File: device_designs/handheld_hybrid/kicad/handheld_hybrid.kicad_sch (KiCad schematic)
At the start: 12 parts, among them U3V3 TPS62864

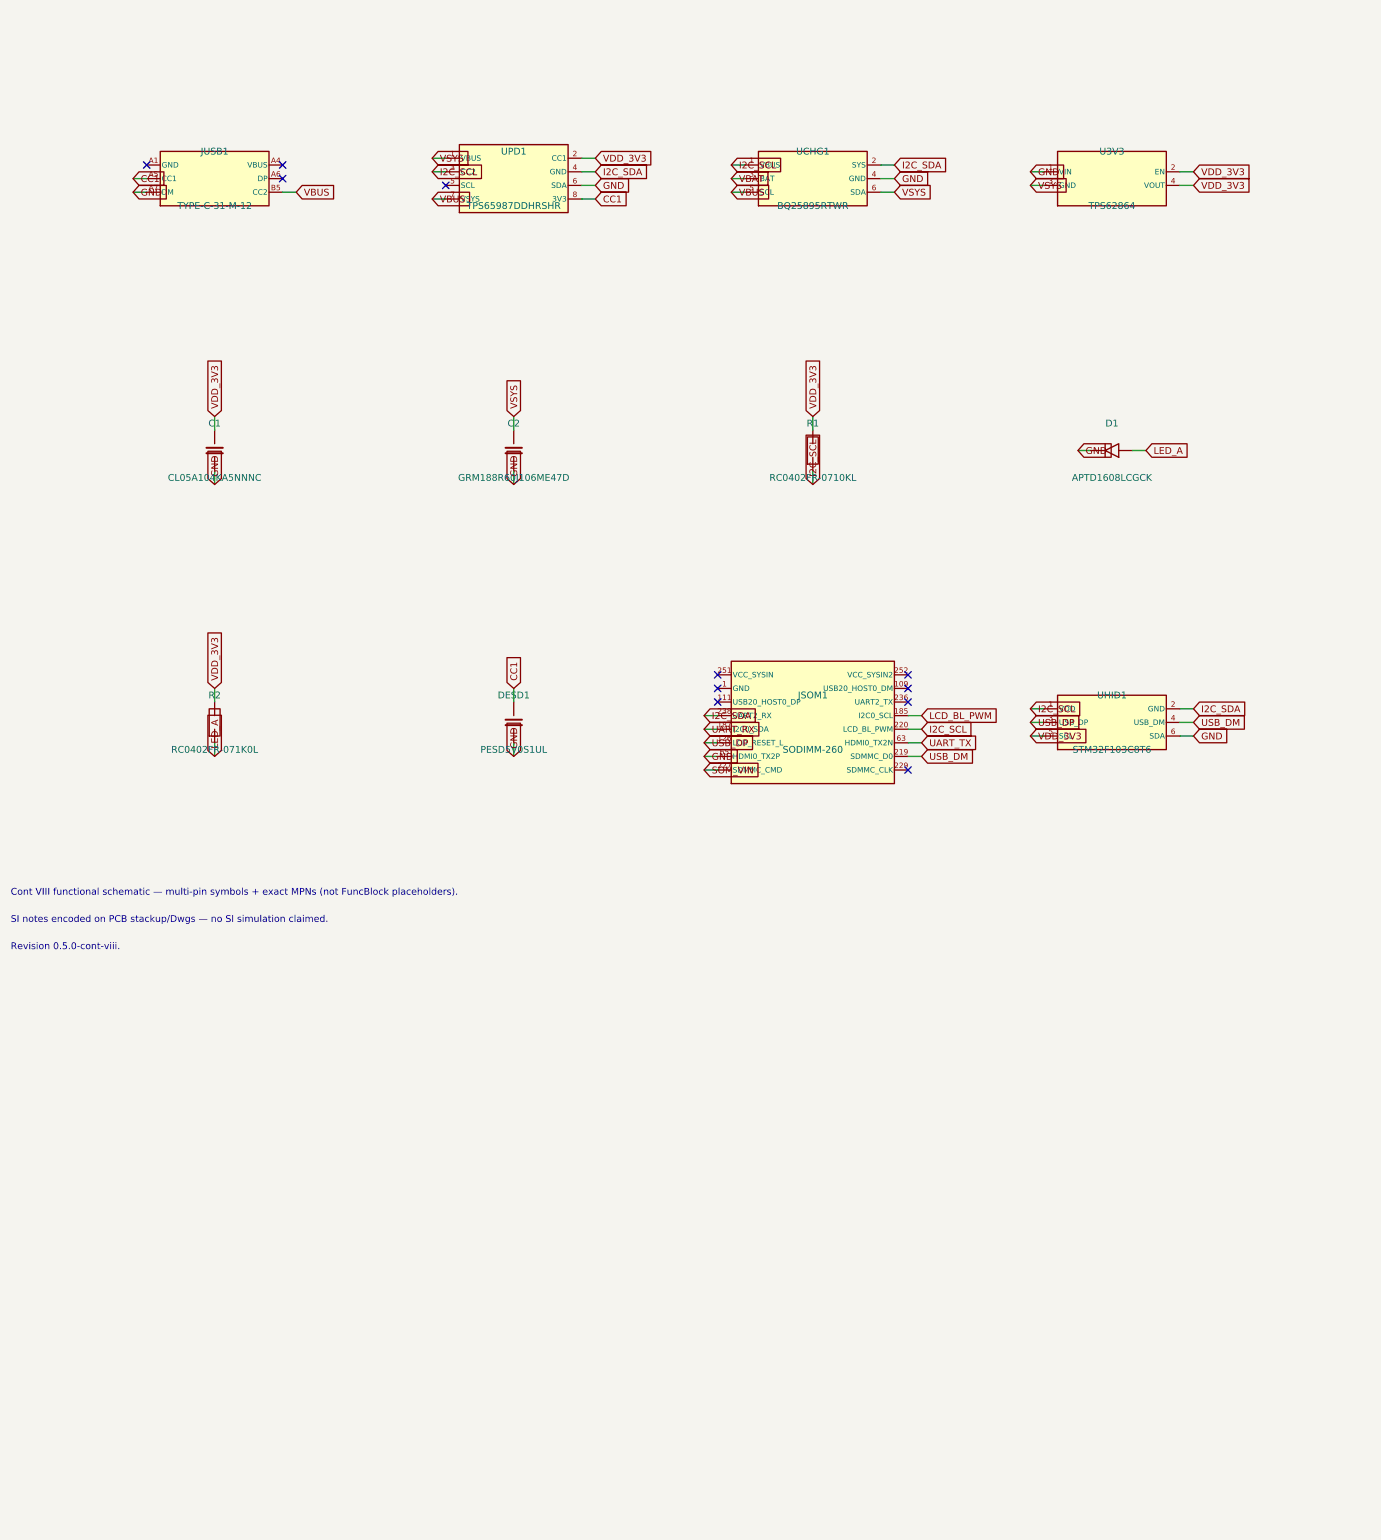
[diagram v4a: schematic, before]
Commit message: feat(eda): Continuation IX Pre-EVT digital release lock for five-product family
Close Cont VIII residual DIGITAL blockers with production footprints, full Radxa 260-pin hierarchical sheets, assembly/RFQ/EVT packages, and honest ADLINK-retained COM-HPC tokens under PHYSICAL_EXECUTION_FREEZE.

Co-authored-by: Cursor <cursoragent@cursor.com>
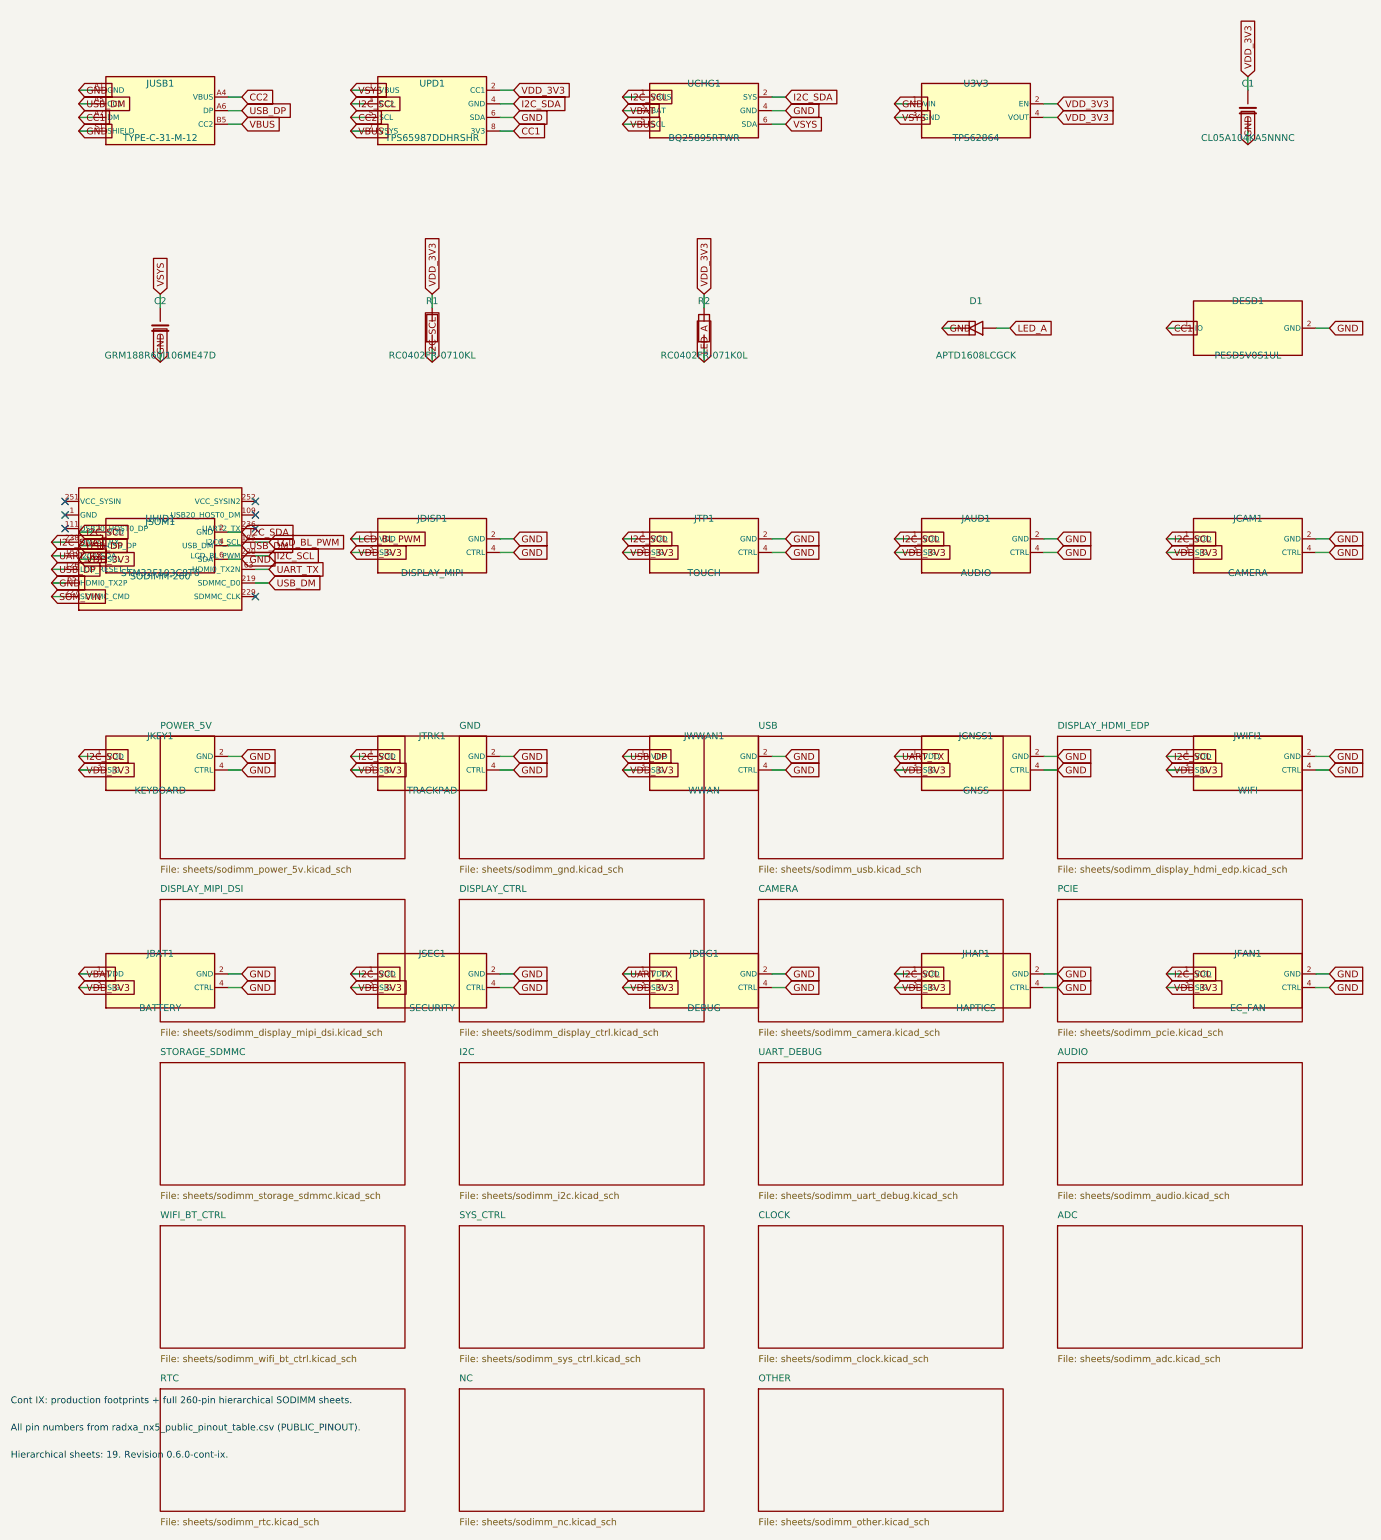
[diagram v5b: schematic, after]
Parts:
- added JAUD1: AUDIO, gunnchos_production:DFN1006-2, symbol PERIPH
- added JBAT1: BATTERY, gunnchos_production:DFN1006-2, symbol PERIPH
- added JCAM1: CAMERA, gunnchos_production:FFC_40P_0.5mm, symbol PERIPH
- added JDBG1: DEBUG, gunnchos_production:DFN1006-2, symbol PERIPH
- added JDISP1: DISPLAY_MIPI, gunnchos_production:FFC_40P_0.5mm, symbol PERIPH
- added JFAN1: EC_FAN, gunnchos_production:DFN1006-2, symbol PERIPH
- added JGNSS1: GNSS, gunnchos_production:DFN1006-2, symbol PERIPH
- added JHAP1: HAPTICS, gunnchos_production:DFN1006-2, symbol PERIPH
- added JKEY1: KEYBOARD, gunnchos_production:DFN1006-2, symbol PERIPH
- added JSEC1: SECURITY, gunnchos_production:DFN1006-2, symbol PERIPH
- added JTP1: TOUCH, gunnchos_production:DFN1006-2, symbol PERIPH
- added JTRK1: TRACKPAD, gunnchos_production:DFN1006-2, symbol PERIPH
- added JWIFI1: WIFI, gunnchos_production:DFN1006-2, symbol PERIPH
- added JWWAN1: WWAN, gunnchos_production:DFN1006-2, symbol PERIPH
- C1, C2: footprint gunnchos_functional:C_0402 -> gunnchos_production:C_0402; ContIX (none) -> PRODUCTION; ContVIII FUNCTIONAL -> (none)
- D1: footprint gunnchos_functional:LED_0603 -> gunnchos_production:LED_0603; ContIX (none) -> PRODUCTION; ContVIII FUNCTIONAL -> (none)
- DESD1: footprint gunnchos_functional:R_0402 -> gunnchos_production:DFN1006-2; symbol C -> ESD; ContIX (none) -> PRODUCTION; ContVIII FUNCTIONAL -> (none)
- JSOM1: footprint gunnchos_functional:Block_SMD_safe -> gunnchos_production:SODIMM-260_DDR4_Socket; ContIX (none) -> PRODUCTION; ContVIII FUNCTIONAL -> (none)
- JUSB1: footprint gunnchos_functional:Block_SMD_safe -> gunnchos_production:USB_C_Receptacle_Production; ContIX (none) -> PRODUCTION; ContVIII FUNCTIONAL -> (none)
- R1, R2: footprint gunnchos_functional:R_0402 -> gunnchos_production:R_0402; ContIX (none) -> PRODUCTION; ContVIII FUNCTIONAL -> (none)
- U3V3: footprint gunnchos_functional:Block_SMD_safe -> gunnchos_production:QFN-16-1EP_3x3mm_P0.5mm; ContIX (none) -> PRODUCTION; ContVIII FUNCTIONAL -> (none)
- UCHG1: footprint gunnchos_functional:Block_SMD_safe -> gunnchos_production:WQFN-24-1EP_4x4mm_P0.5mm; ContIX (none) -> PRODUCTION; ContVIII FUNCTIONAL -> (none)
- UHID1: footprint gunnchos_functional:Block_SMD_safe -> gunnchos_production:LQFP-48_7x7mm_P0.5mm; ContIX (none) -> PRODUCTION; ContVIII FUNCTIONAL -> (none)
- UPD1: footprint gunnchos_functional:Block_SMD_safe -> gunnchos_production:VQFN-56-1EP_7x7mm_P0.4mm; ContIX (none) -> PRODUCTION; ContVIII FUNCTIONAL -> (none)
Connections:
- net CC1: now also JUSB1.A7 (DM); no longer JUSB1.A5 (CC1)
- net GND: now also JUSB1.A1 (GND), JUSB1.S1 (SHIELD), JAUD1.2 (GND), JAUD1.4 (CTRL), JBAT1.2 (GND), JBAT1.4 (CTRL), JCAM1.2 (GND), JCAM1.4 (CTRL), JDBG1.2 (GND), JDBG1.4 (CTRL), JDISP1.2 (GND), JDISP1.4 (CTRL), JFAN1.2 (GND), JFAN1.4 (CTRL), JGNSS1.2 (GND), JGNSS1.4 (CTRL), JHAP1.2 (GND), JHAP1.4 (CTRL), JKEY1.2 (GND), JKEY1.4 (CTRL), JSEC1.2 (GND), JSEC1.4 (CTRL), JTP1.2 (GND), JTP1.4 (CTRL), JTRK1.2 (GND), JTRK1.4 (CTRL), JWIFI1.2 (GND), JWIFI1.4 (CTRL), JWWAN1.2 (GND), JWWAN1.4 (CTRL); no longer JUSB1.A7 (DM)
- net I2C_SCL: now also JAUD1.1 (VDD), JCAM1.1 (VDD), JFAN1.1 (VDD), JHAP1.1 (VDD), JKEY1.1 (VDD), JSEC1.1 (VDD), JTP1.1 (VDD), JTRK1.1 (VDD), JWIFI1.1 (VDD)
- net LCD_BL_PWM: now also JDISP1.1 (VDD)
- net UART_TX: now also JDBG1.1 (VDD), JGNSS1.1 (VDD)
- net USB_DM: now also JUSB1.A5 (CC1)
- net USB_DP: now also JUSB1.A6 (DP), JWWAN1.1 (VDD)
- net VBAT: now also JBAT1.1 (VDD)
- net VDD_3V3: now also JAUD1.3 (SIG), JBAT1.3 (SIG), JCAM1.3 (SIG), JDBG1.3 (SIG), JDISP1.3 (SIG), JFAN1.3 (SIG), JGNSS1.3 (SIG), JHAP1.3 (SIG), JKEY1.3 (SIG), JSEC1.3 (SIG), JTP1.3 (SIG), JTRK1.3 (SIG), JWIFI1.3 (SIG), JWWAN1.3 (SIG)
- net CC2: now reaches UPD1.5 (SCL)
- net CC2: now also JUSB1.A4 (VBUS)
- no-connect marks 11 -> 7
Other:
- added sheet ADC (sheets/sodimm_adc.kicad_sch)
- added sheet AUDIO (sheets/sodimm_audio.kicad_sch)
- added sheet CAMERA (sheets/sodimm_camera.kicad_sch)
- added sheet CLOCK (sheets/sodimm_clock.kicad_sch)
- added sheet DISPLAY_CTRL (sheets/sodimm_display_ctrl.kicad_sch)
- added sheet DISPLAY_HDMI_EDP (sheets/sodimm_display_hdmi_edp.kicad_sch)
- added sheet DISPLAY_MIPI_DSI (sheets/sodimm_display_mipi_dsi.kicad_sch)
- added sheet GND (sheets/sodimm_gnd.kicad_sch)
- added sheet I2C (sheets/sodimm_i2c.kicad_sch)
- added sheet NC (sheets/sodimm_nc.kicad_sch)
- added sheet OTHER (sheets/sodimm_other.kicad_sch)
- added sheet PCIE (sheets/sodimm_pcie.kicad_sch)
- added sheet POWER_5V (sheets/sodimm_power_5v.kicad_sch)
- added sheet RTC (sheets/sodimm_rtc.kicad_sch)
- added sheet STORAGE_SDMMC (sheets/sodimm_storage_sdmmc.kicad_sch)
- added sheet SYS_CTRL (sheets/sodimm_sys_ctrl.kicad_sch)
- added sheet UART_DEBUG (sheets/sodimm_uart_debug.kicad_sch)
- added sheet USB (sheets/sodimm_usb.kicad_sch)
- added sheet WIFI_BT_CTRL (sheets/sodimm_wifi_bt_ctrl.kicad_sch)
- note added: "All pin numbers from radxa_nx5_public_pinout_table.csv (PUBLIC_PINOUT)."
- note added: "Cont IX: production footprints + full 260-pin hierarchical SODIMM sheets."
- note added: "Hierarchical sheets: 19. Revision 0.6.0-cont-ix."
- note removed: "Cont VIII functional schematic — multi-pin symbols + exact MPNs (not FuncBlock placeholders)."
- note removed: "Revision 0.5.0-cont-viii."
- note removed: "SI notes encoded on PCB stackup/Dwgs — no SI simulation claimed."
- company: gunnchOS3k / CONTINUATION VIII -> gunnchOS3k / CONTINUATION IX
- title: Handheld Hybrid SoM Carrier — Cont VIII PUBLIC_PINOUT -> Handheld Hybrid SoM Carrier — Cont IX Pre-EVT
- moved on the sheet: C1, C2, D1, JSOM1, R1, R2, U3V3, UCHG1, UHID1, UPD1
